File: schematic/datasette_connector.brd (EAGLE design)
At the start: 24.3 x 17.8 mm, 3 parts, among them CN1 C64_CASETTE_EDGE, CN3 C64_CASETTE_CONN

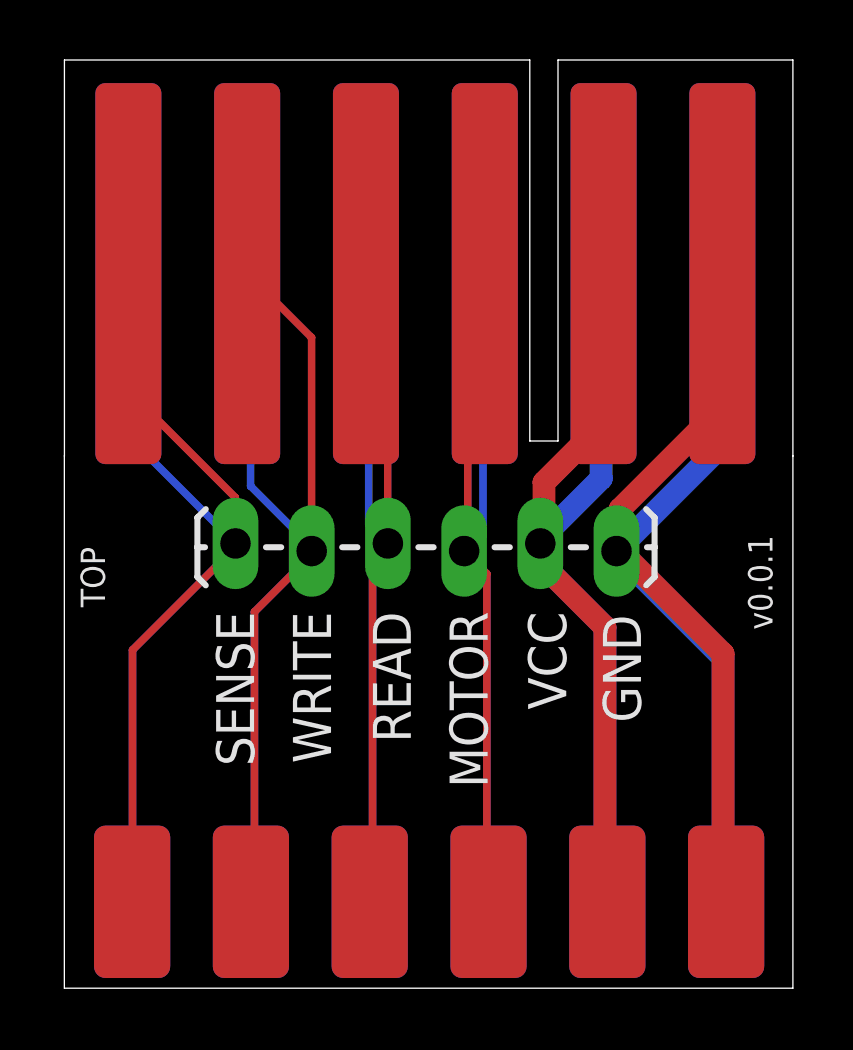
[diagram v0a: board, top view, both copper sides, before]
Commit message: board: datasette: adds panelized version
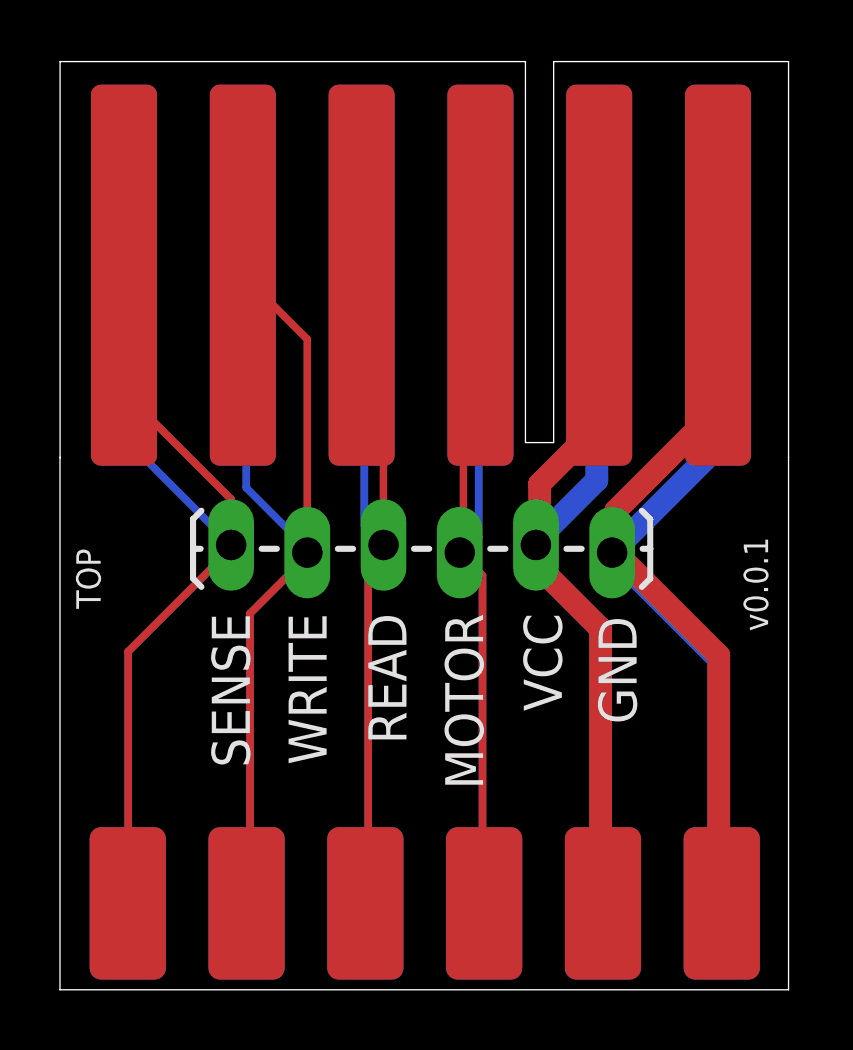
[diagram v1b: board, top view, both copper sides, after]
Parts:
- moved CN1 0.15 mm to (0.15, 23.3)
- moved CN3 0.15 mm to (0.28, -0.80)
- moved JP 0.15 mm to (18.4, 14.6)
